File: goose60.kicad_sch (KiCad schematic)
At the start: 31 parts, among them SW1 SW_Push, SW2 SW_Push, U1 STM32F103CBTx, X1 Crystal_GND24

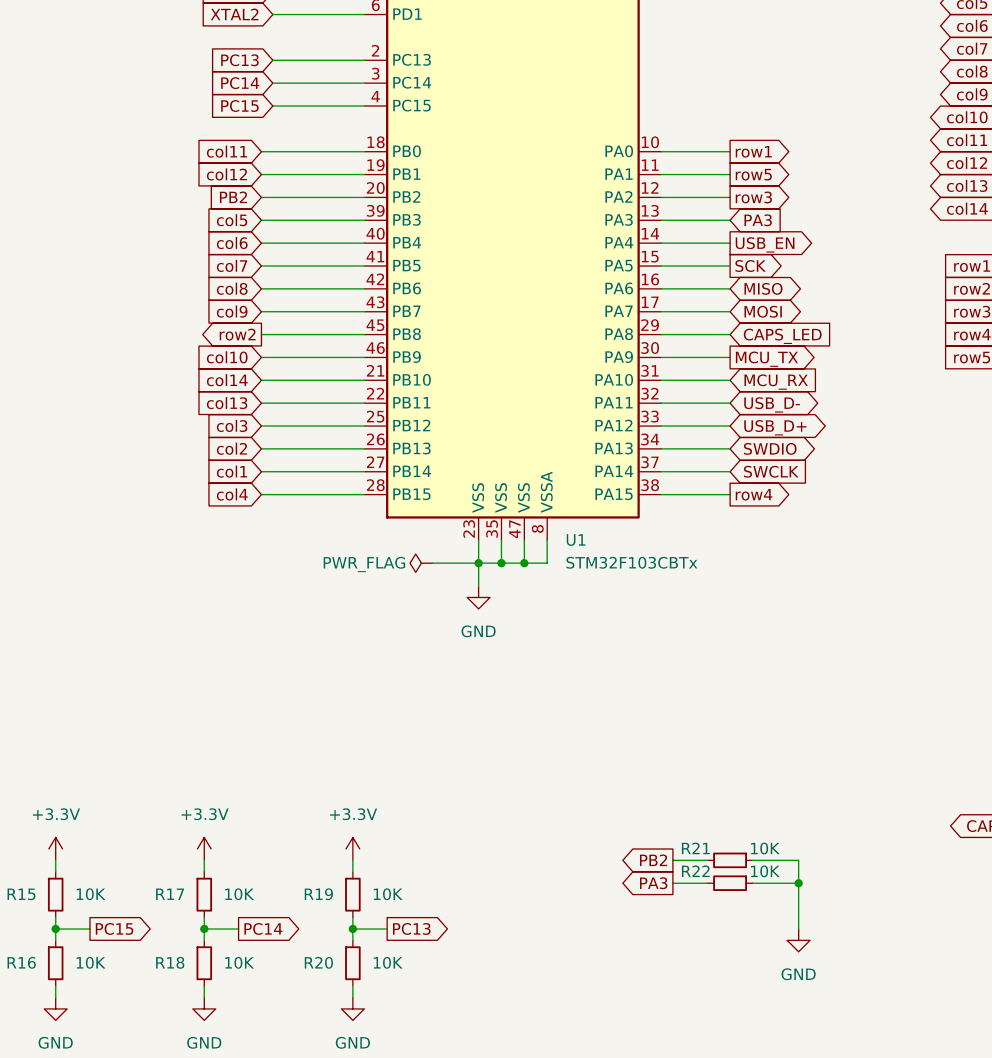
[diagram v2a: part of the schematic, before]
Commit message: add gh60  mechanism hole
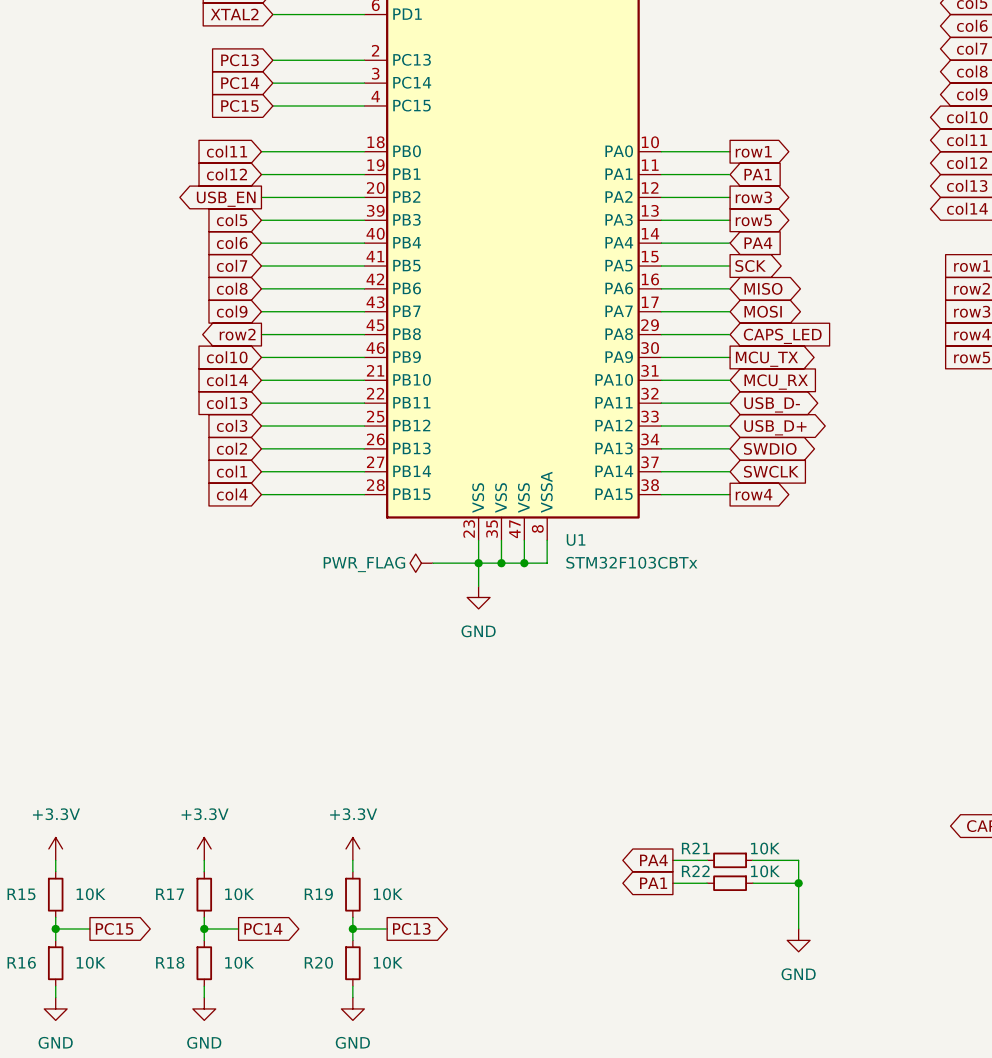
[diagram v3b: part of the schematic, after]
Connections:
- net USB_EN: now also U1.20 (PB2); no longer U1.14 (PA4)
- net row5: now also U1.13 (PA3); no longer U1.11 (PA1)
- net PA3 renamed PA1
- net PA1: now also U1.11 (PA1); no longer U1.13 (PA3)
- net PB2 renamed PA4
- net PA4: now also U1.14 (PA4); no longer U1.20 (PB2)
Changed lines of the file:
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@@
-    )
-  )
-  (global_label "PA3" (shape input) (at 208.28 72.39 0) (fields_autoplaced)
-    (effects (font (size 1.27 1.27)) (justify left))
-    (property "插入圖紙頁參考" "${INTERSHEET_REFS}" (id 0) (at 214.2612 72.3106 0)
-      (effects (font (size 1.27 1.27)) (justify left) hide)
     )
   )
@@
     )
   )
-  (global_label "row5" (shape output) (at 208.28 67.31 0) (fields_autoplaced)
-    (effects (font (size 1.27 1.27)) (justify left))
-    (property "插入圖紙頁參考" "${INTERSHEET_REFS}" (id 0) (at 215.1683 67.2306 0)
-      (effects (font (size 1.27 1.27)) (justify left) hide)
-    )
-  )
   (global_label "col5" (shape input) (at 156.21 72.39 180) (fields_autoplaced)
     (effects (font (size 1.27 1.27)) (justify right))
@@
     )
   )
+  (global_label "USB_EN" (shape output) (at 156.21 69.85 180) (fields_autoplaced)
+    (effects (font (size 1.27 1.27)) (justify right))
+    (property "插入圖紙頁參考" "${INTERSHEET_REFS}" (id 0) (at 146.5398 69.9294 0)
+      (effects (font (size 1.27 1.27)) (justify right) hide)
+    )
+  )
   (global_label "col14" (shape output) (at 237.49 71.12 180) (fields_autoplaced)
     (effects (font (size 1.27 1.27)) (justify right))
@@
     )
   )
-  (global_label "PB2" (shape output) (at 201.93 143.51 180) (fields_autoplaced)
-    (effects (font (size 1.27 1.27)) (justify right))
-    (property "插入圖紙頁參考" "${INTERSHEET_REFS}" (id 0) (at 195.7674 143.4306 0)
+  (global_label "PA4" (shape output) (at 201.93 143.51 180) (fields_autoplaced)
+    (effects (font (size 1.27 1.27)) (justify right))
+    (property "插入圖紙頁參考" "${INTERSHEET_REFS}" (id 0) (at 195.9488 143.4306 0)
       (effects (font (size 1.27 1.27)) (justify right) hide)
     )
@@
     )
   )
-  (global_label "PA3" (shape output) (at 201.93 146.05 180) (fields_autoplaced)
+  (global_label "PA1" (shape output) (at 201.93 146.05 180) (fields_autoplaced)
     (effects (font (size 1.27 1.27)) (justify right))
     (property "插入圖紙頁參考" "${INTERSHEET_REFS}" (id 0) (at 195.9488 145.9706 0)
@@
     )
   )
+  (global_label "PA1" (shape input) (at 208.28 67.31 0) (fields_autoplaced)
+    (effects (font (size 1.27 1.27)) (justify left))
+    (property "插入圖紙頁參考" "${INTERSHEET_REFS}" (id 0) (at 214.2612 67.2306 0)
+      (effects (font (size 1.27 1.27)) (justify left) hide)
+    )
+  )
   (global_label "RESET" (shape output) (at 58.42 138.43 0) (fields_autoplaced)
     (effects (font (size 1.27 1.27)) (justify left))
@@
     )
   )
-  (global_label "PB2" (shape input) (at 156.21 69.85 180) (fields_autoplaced)
-    (effects (font (size 1.27 1.27)) (justify right))
-    (property "插入圖紙頁參考" "${INTERSHEET_REFS}" (id 0) (at 150.0474 69.7706 0)
-      (effects (font (size 1.27 1.27)) (justify right) hide)
-    )
-  )
   (global_label "col12" (shape output) (at 237.49 66.04 180) (fields_autoplaced)
     (effects (font (size 1.27 1.27)) (justify right))
@@
     )
   )
+  (global_label "PA4" (shape input) (at 208.28 74.93 0) (fields_autoplaced)
+    (effects (font (size 1.27 1.27)) (justify left))
+    (property "插入圖紙頁參考" "${INTERSHEET_REFS}" (id 0) (at 214.2612 74.8506 0)
+      (effects (font (size 1.27 1.27)) (justify left) hide)
+    )
+  )
   (global_label "col6" (shape input) (at 156.21 74.93 180) (fields_autoplaced)
     (effects (font (size 1.27 1.27)) (justify right))
@@
     )
   )
+  (global_label "row5" (shape output) (at 208.28 72.39 0) (fields_autoplaced)
+    (effects (font (size 1.27 1.27)) (justify left))
+    (property "插入圖紙頁參考" "${INTERSHEET_REFS}" (id 0) (at 215.1683 72.3106 0)
+      (effects (font (size 1.27 1.27)) (justify left) hide)
+    )
+  )
   (global_label "col5" (shape output) (at 237.49 48.26 180) (fields_autoplaced)
     (effects (font (size 1.27 1.27)) (justify right))
@@
     )
   )
-  (global_label "USB_EN" (shape output) (at 208.28 74.93 0) (fields_autoplaced)
-    (effects (font (size 1.27 1.27)) (justify left))
-    (property "插入圖紙頁參考" "${INTERSHEET_REFS}" (id 0) (at 217.9502 74.8506 0)
-      (effects (font (size 1.27 1.27)) (justify left) hide)
-    )
-  )

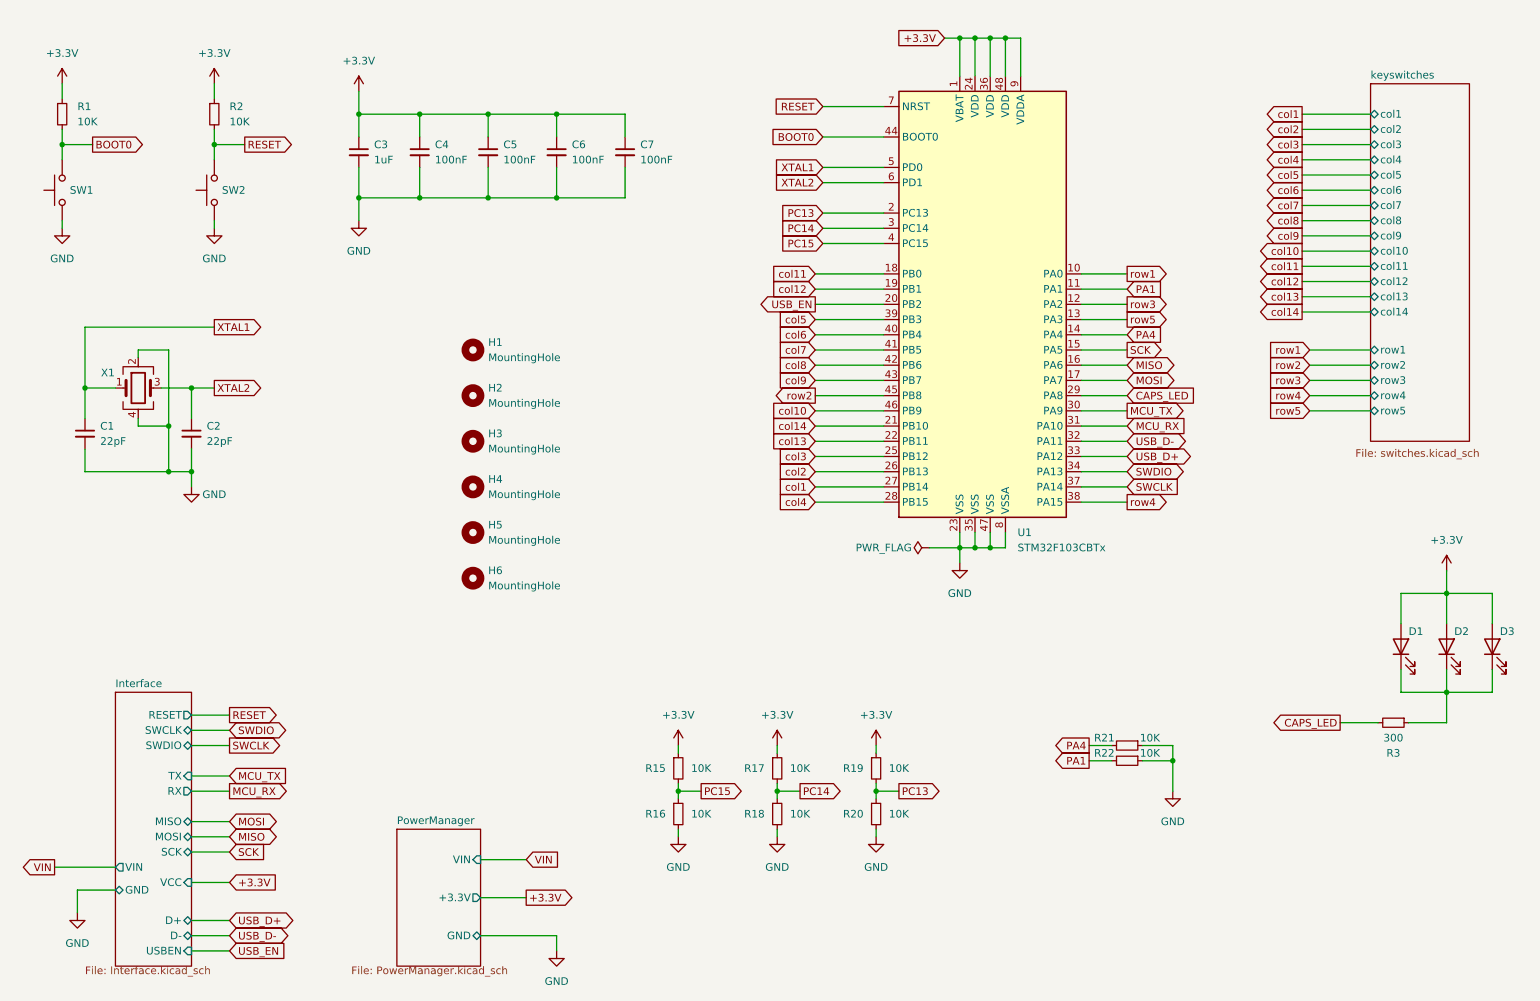
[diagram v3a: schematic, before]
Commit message: modify power/bootload circuit
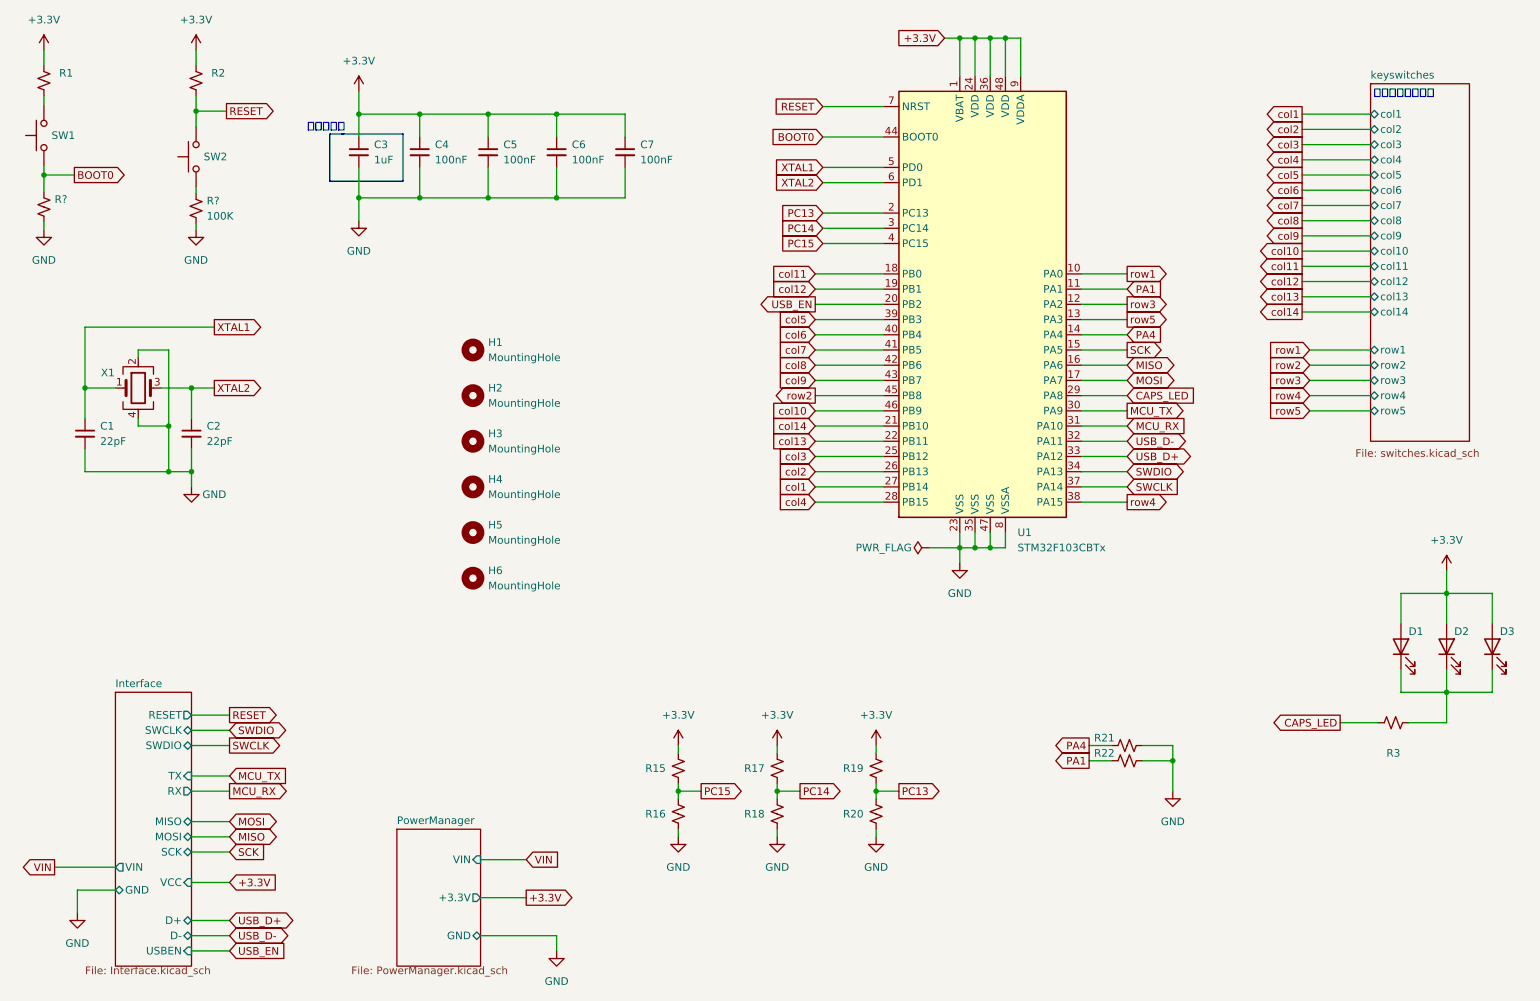
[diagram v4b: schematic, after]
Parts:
- added R?: (no value), Resistor_SMD:R_0603_1608Metric, symbol Device:R_Small_US
- added R?: 100K, Resistor_SMD:R_0603_1608Metric, symbol Device:R_Small_US
- R1, R15, R16, R17, R18, R19, R2, R20, R21, R22: value 10K -> (none); footprint Resistor_SMD:R_0603_1608Metric -> (none); symbol Device:R_Small -> Device:R_Small_US
- R3: value 300 -> (none); footprint Resistor_SMD:R_0603_1608Metric -> (none); symbol Device:R_Small -> Device:R_Small_US
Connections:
- net BOOT0: now also SW1.1, R?.1; no longer R1.2, SW1.2
- net GND: now also R?.2, R?.2; no longer SW1.1, SW2.1
- new net: R1.2, SW1.2
- new net: R?.1, SW2.1
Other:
- note added: "二極體封裝要修正"
- note added: "封裝需確認"
- moved on the sheet: SW1, SW2

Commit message: modify pcb footprint
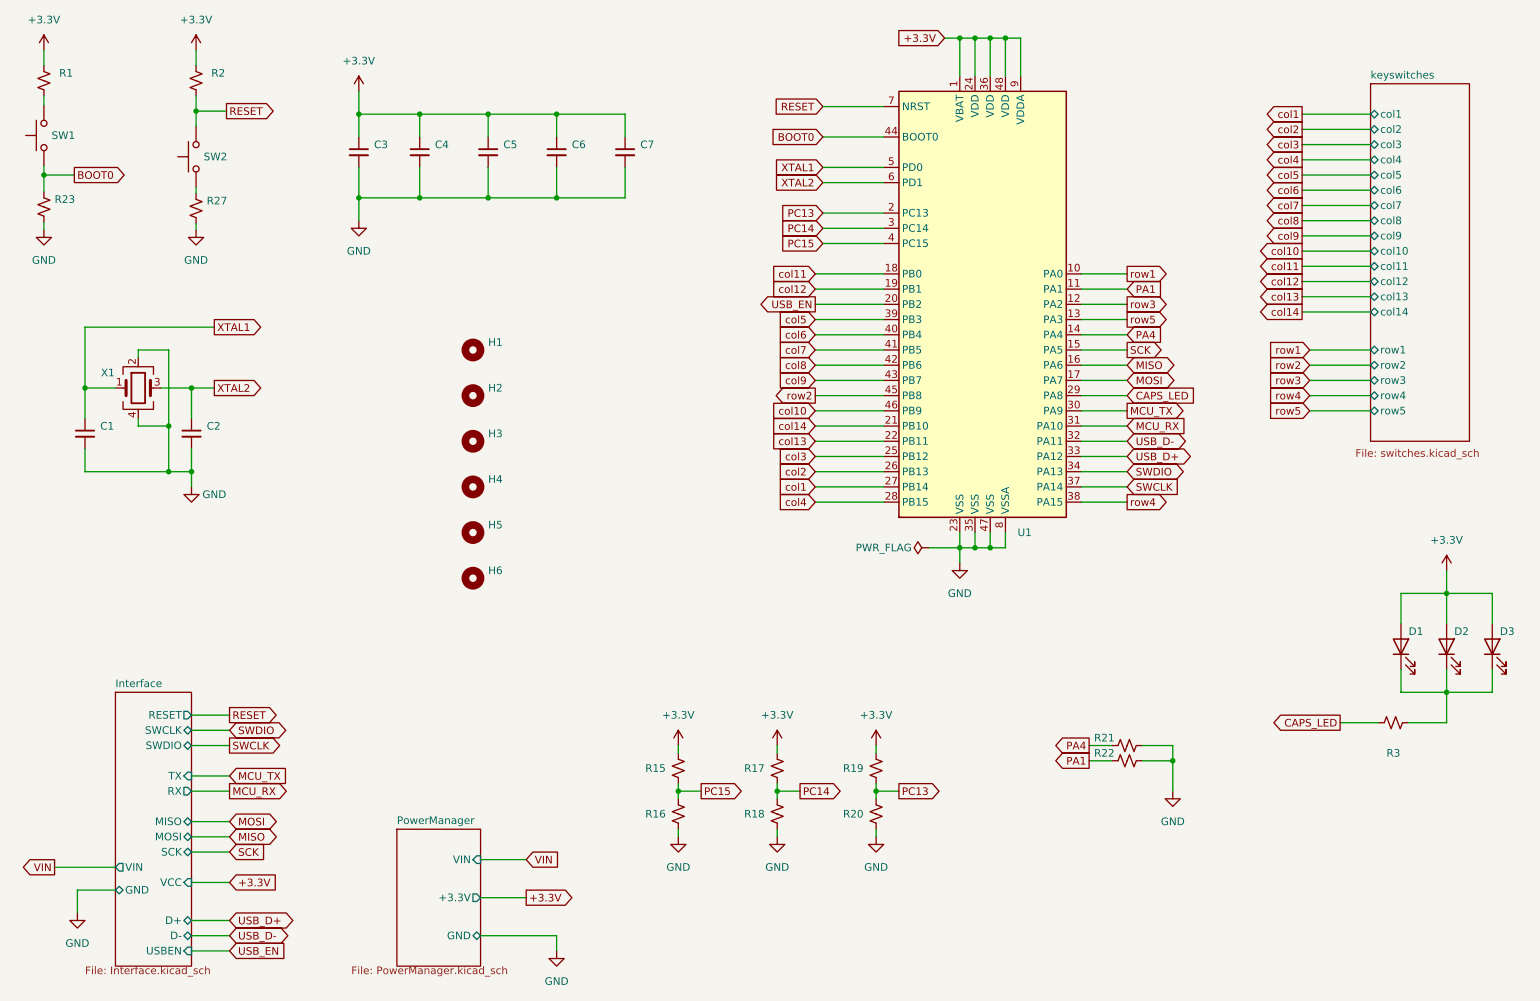
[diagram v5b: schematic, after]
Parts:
- C1, C2: value 22pF -> (none); footprint Capacitor_SMD:C_0603_1608Metric -> (none)
- C3: value 1uF -> (none); footprint Capacitor_SMD:C_0603_1608Metric -> (none)
- C4, C5, C6, C7: value 100nF -> (none); footprint Capacitor_SMD:C_0603_1608Metric -> (none)
- D1, D2, D3: value LED -> (none); footprint LED_SMD:LED_0805_2012Metric -> (none)
- H1: value MountingHole -> (none); footprint MountingHole:MountingHole_3.2mm_M3_Pad -> (none)
- H2, H3, H4, H5, H6: value MountingHole -> (none); footprint MountingHole:MountingHole_3.2mm_M3_Pad_TopOnly -> (none)
- R23: renamed from R?; footprint Resistor_SMD:R_0603_1608Metric -> (none)
- R27: renamed from R?; value 100K -> (none); footprint Resistor_SMD:R_0603_1608Metric -> (none)
- SW1, SW2: value SW_Push -> (none); footprint Button_Switch_SMD:SW_Push_1P1T_NO_CK_KSC6xxJ -> (none)
- U1: value STM32F103CBTx -> (none); footprint Package_QFP:LQFP-48_7x7mm_P0.5mm -> (none)
- X1: value Crystal_GND24 -> (none); footprint Crystal:Crystal_SMD_TXC_7M-4Pin_3.2x2.5mm -> (none)
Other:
- note removed: "二極體封裝要修正"
- note removed: "封裝需確認"
